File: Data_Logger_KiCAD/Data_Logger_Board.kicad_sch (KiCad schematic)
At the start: 15 parts, among them J1 Conn_Coaxial, U1 SX1262IMLTRT, U2 MASW-007221, Y1 Crystal_GND23

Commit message: Sub-schematics Generated
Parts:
- removed C1, C2, C3, C4: 100n, symbol Device:C
- removed C5, C6: 1n, symbol Device:C
- removed FL1: 0900FM15K0039, RF_Converter:Balun_Johanson_0900FM15K0039, symbol Filter:0900FM15K0039
- removed J1: Conn_Coaxial, symbol Connector:Conn_Coaxial
- removed L1, L2: L, symbol Device:L
- removed R1, R2: 100, symbol Device:R
- removed U1: SX1262IMLTRT, Package_DFN_QFN:QFN-24-1EP_4x4mm_P0.5mm_EP2.6x2.6mm, symbol RF:SX1262IMLTRT
- removed U2: MASW-007221, Package_TO_SOT_SMD:SOT-363_SC-70-6, symbol RF_Switch:MASW-007221
- removed Y1: Crystal_GND23, symbol Device:Crystal_GND23
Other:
- sheet BAROMETER ports: added CSB_BMP, CSB_MS, SCK, SDI, SDO; removed none
- sheet Magnetometer ports: added INT, SCL/SPI_SCK, SDA/SPI_SDI, SPI_CS, SPI_SDO; removed none

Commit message: Radio Layout V1.0
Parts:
- added J1: Conn_Coaxial, Connector_Coaxial:SMA_Amphenol_132289_EdgeMount, symbol Connector:Conn_Coaxial
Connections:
- net RF_LORA/SMA_CONN: now also J1.1 (In)
- new net GND: J1.2 (Ext)
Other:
- sheet GPS ports: added Antenna, EXTINT, SCL, SDA; removed none
- sheet RF_LORA ports: added none; removed DIO3

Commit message: minor updates
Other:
- sheet GPS ports: added TIMEPULSE; removed Antenna
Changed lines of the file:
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@@
-			)
-		)
-		(pin "Antenna" input
-			(at 217.17 40.64 0)
-			(effects
-				(font
-					(size 1.27 1.27)
-				)
-				(justify right)
 			)
 		)
@@
 			)
 		)
-		(pin "SDA" input
+		(pin "SDA" bidirectional
 			(at 179.07 45.72 180)
 			(effects
@@
 			)
 		)
+		(pin "TIMEPULSE" output
+			(at 217.17 45.72 0)
+			(effects
+				(font
+					(size 1.27 1.27)
+				)
+				(justify right)
+			)
+		)

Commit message: updates
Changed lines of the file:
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@@
-			)
-		)
-		(pin "MISO" input
-			(at 66.04 137.16 180)
-			(effects
-				(font
-					(size 1.27 1.27)
-				)
-				(justify left)
 			)
 		)
@@
 			(effects
 				(font
+					(size 1.27 1.27)
+				)
+				(justify right)
+			)
+		)
+		(pin "MISO" output
+			(at 107.95 130.81 0)
+			(effects
+				(font

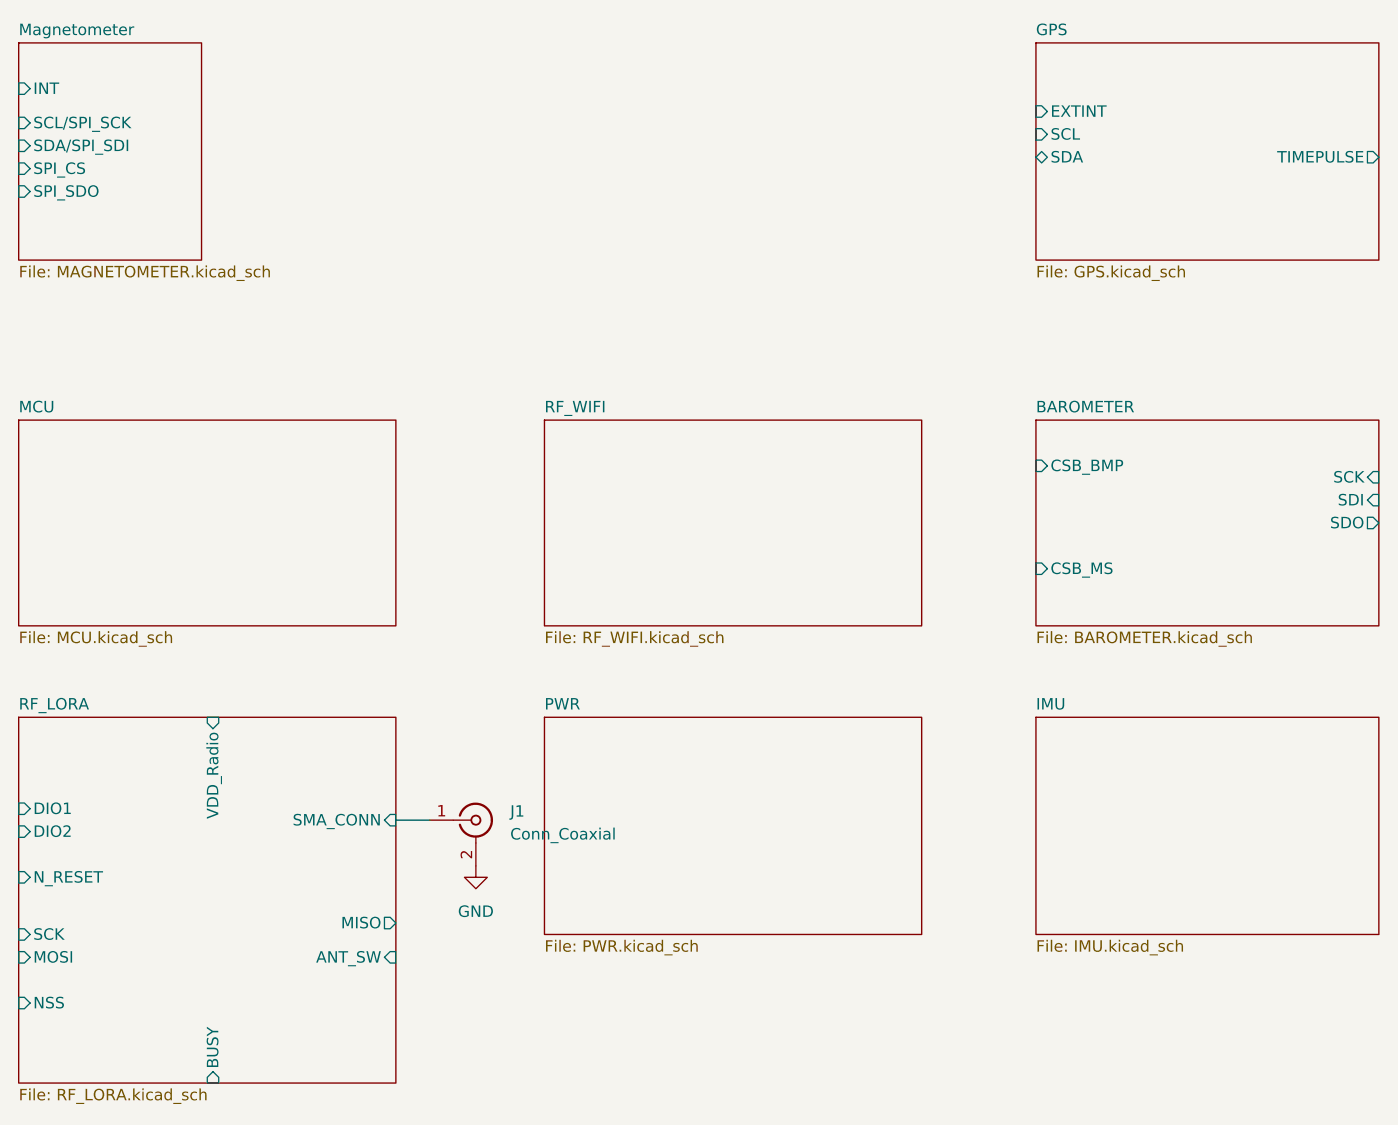
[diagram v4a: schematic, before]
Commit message: Aggregated sub schematics into single primary schematic
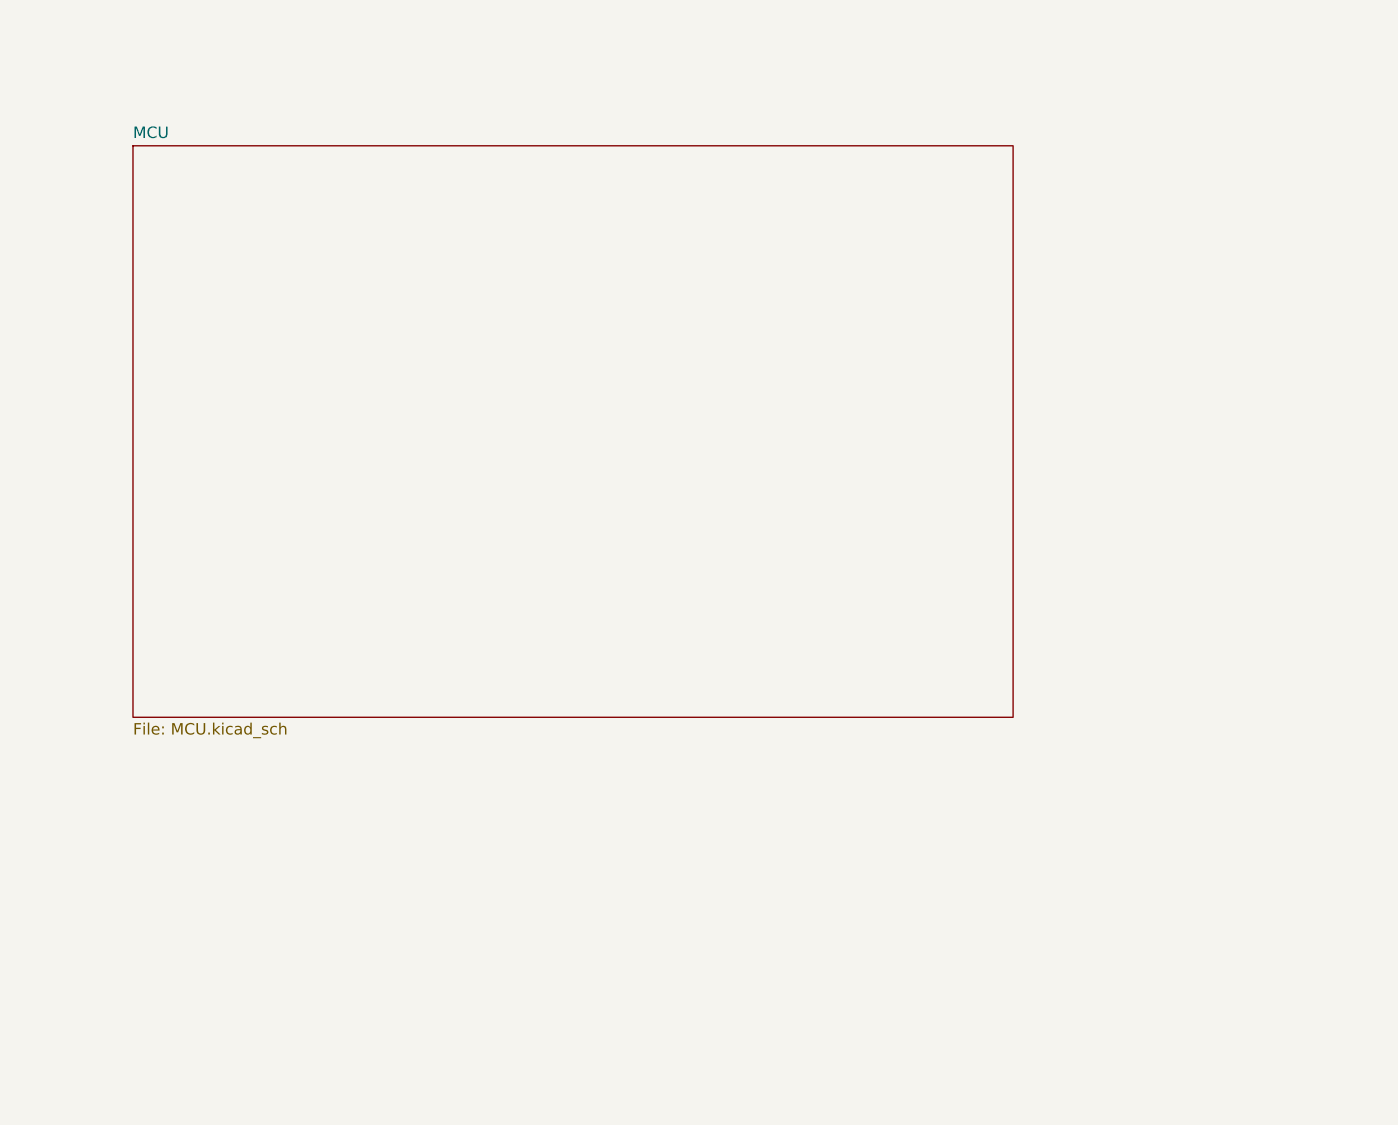
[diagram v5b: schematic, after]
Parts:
- removed J1: Conn_Coaxial, Connector_Coaxial:SMA_Amphenol_132289_EdgeMount, symbol Connector:Conn_Coaxial
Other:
- removed sheet BAROMETER
- removed sheet GPS
- removed sheet IMU
- removed sheet Magnetometer
- removed sheet PWR
- removed sheet RF_LORA
- removed sheet RF_WIFI
